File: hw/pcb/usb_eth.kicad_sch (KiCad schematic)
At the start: 39 parts, among them U5 93AAxxAT-xOT, U6 LAN7801

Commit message: whisperbounce: assign footprints
Signed-off-by: Dominik Sliwa <dominik@sliwa.io>
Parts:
- C20, C22, C23, C24, C25, C26, C27, C28, C29, C30, C31, C32, C33, C34, C35, C36, C37, C38, C39, C40, C41, C42: footprint (none) -> Capacitor_SMD:C_0402_1005Metric
- C43: footprint (none) -> Capacitor_SMD:C_0805_2012Metric
- FB1, FB3, FB4: footprint (none) -> Resistor_SMD:R_0603_1608Metric
- L1: footprint (none) -> Inductor_SMD:L_Taiyo-Yuden_NR-40xx_HandSoldering
- R10, R11, R12, R13, R14, R15, R16: footprint (none) -> Resistor_SMD:R_0402_1005Metric
- RN2, RN3, RN4: footprint (none) -> Resistor_SMD:R_Array_Convex_4x0402
- U6: footprint (none) -> Package_DFN_QFN:QFN-64-1EP_9x9mm_P0.5mm_EP6x6mm_ThermalVias

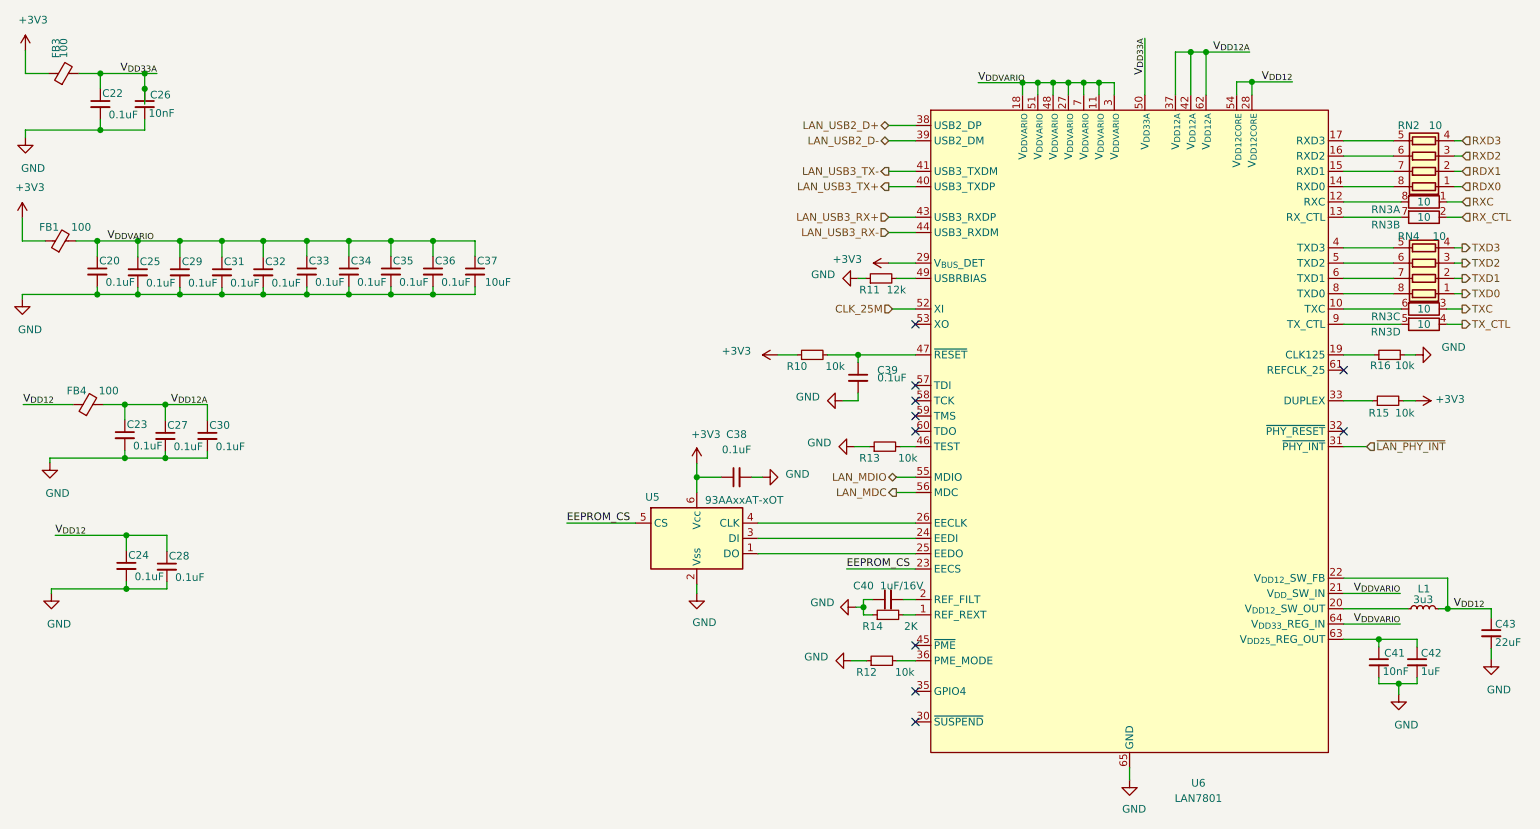
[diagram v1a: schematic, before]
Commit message: whisperbounce: pcb v1
Includes schematic and assigment tweaks

Signed-off-by: Dominik Sliwa <dominik@sliwa.io>
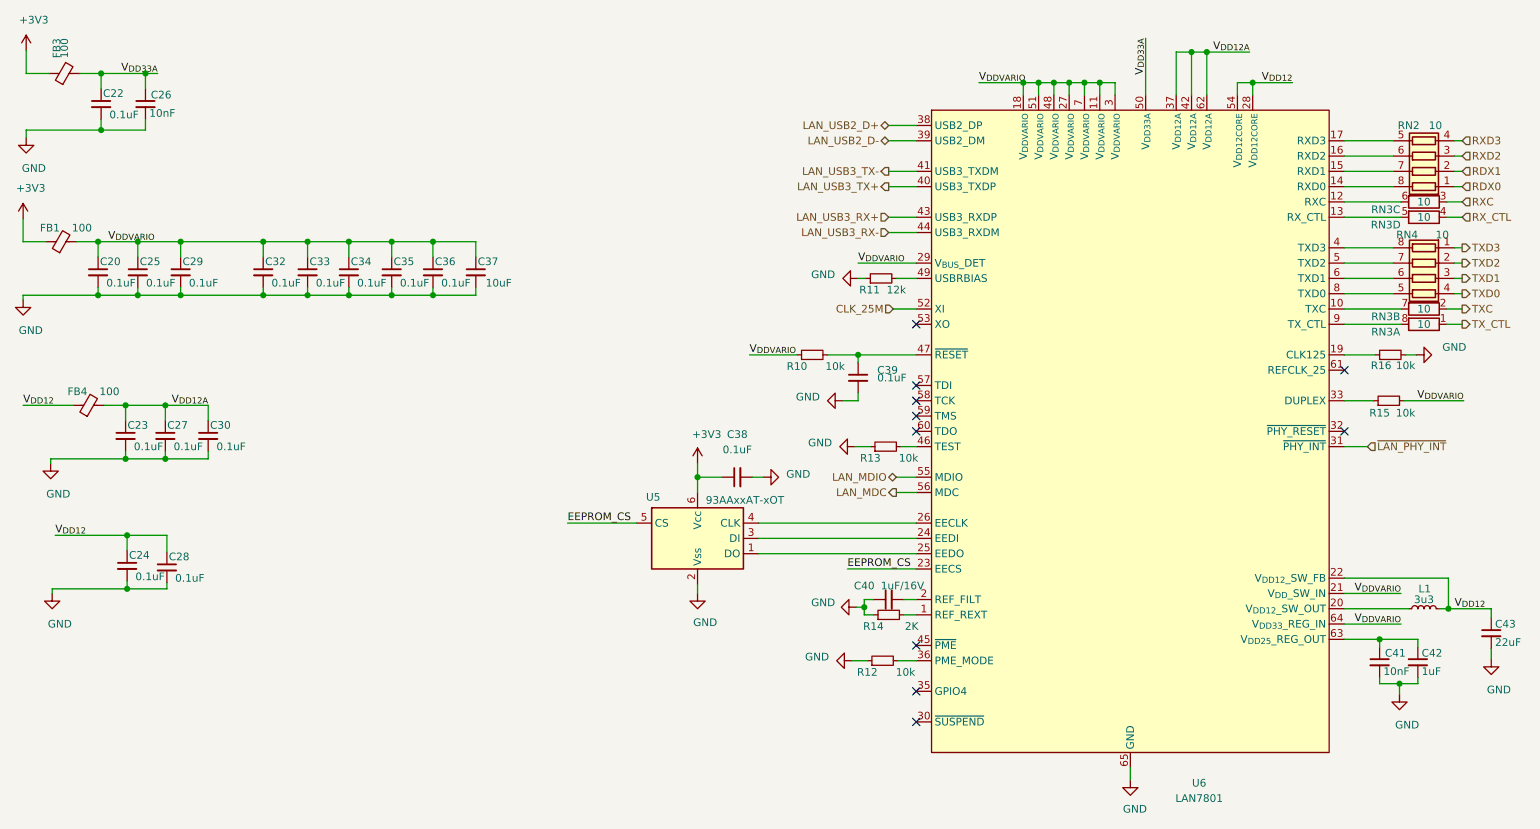
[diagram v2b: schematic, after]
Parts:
- removed C31: 0.1uF, Capacitor_SMD:C_0402_1005Metric, symbol Device:C_Small
- L1: footprint Inductor_SMD:L_Taiyo-Yuden_NR-40xx_HandSoldering -> Inductor_SMD:L_Taiyo-Yuden_MD-2020
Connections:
- net +3V3: no longer R10.1, R15.2, U6.29 (V_{BUS}_DET)
- net RXC: now also RN3.3 (R3.1); no longer RN3.1 (R1.1)
- net RX_CTL: now also RN3.4 (R4.1); no longer RN3.2 (R2.1)
- net TXC: now also RN3.2 (R2.1); no longer RN3.3 (R3.1)
- net TXD0: now also RN4.4 (R4.1); no longer RN4.1 (R1.1)
- net TXD1: now also RN4.3 (R3.1); no longer RN4.2 (R2.1)
- net TXD2: now also RN4.2 (R2.1); no longer RN4.3 (R3.1)
- net TXD3: now also RN4.1 (R1.1); no longer RN4.4 (R4.1)
- net TX_CTL: now also RN3.1 (R1.1); no longer RN3.4 (R4.1)
- net V_{DDVARIO}: now also R10.1, R15.2, U6.29 (V_{BUS}_DET)
- net at RN4.5 (R4.2): now also U6.8 (TXD0); no longer U6.4 (TXD3)
- net at RN4.6 (R3.2): now also U6.6 (TXD1); no longer U6.5 (TXD2)
- net at RN4.7 (R2.2): now also U6.5 (TXD2); no longer U6.6 (TXD1)
- net at RN4.8 (R1.2): now also U6.4 (TXD3); no longer U6.8 (TXD0)
- net at U6.10 (TXC): now also RN3.7 (R2.2); no longer RN3.6 (R3.2)
- net at U6.12 (RXC): now also RN3.6 (R3.2); no longer RN3.8 (R1.2)
- net at U6.13 (RX_CTL): now also RN3.5 (R4.2); no longer RN3.7 (R2.2)
- net at U6.9 (TX_CTL): now also RN3.8 (R1.2); no longer RN3.5 (R4.2)
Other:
- moved on the sheet: RN3A, RN3B, RN3C, RN3D
